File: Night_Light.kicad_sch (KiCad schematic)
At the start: 6 parts, among them Q1 2N3904

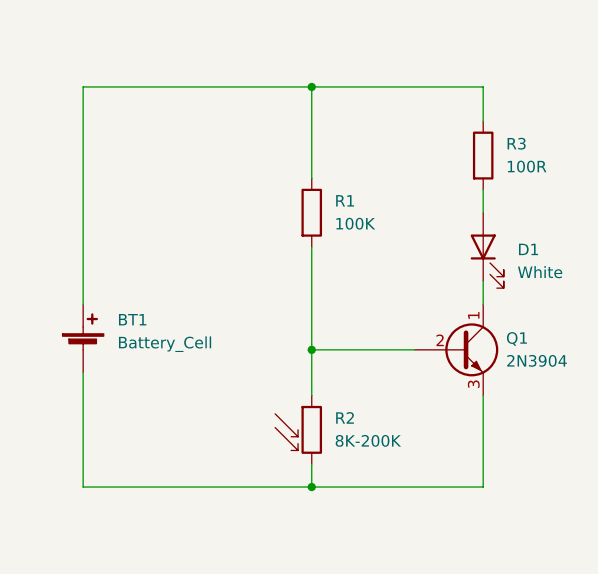
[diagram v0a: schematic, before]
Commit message: Switched battery for connector, add labels, add power flags
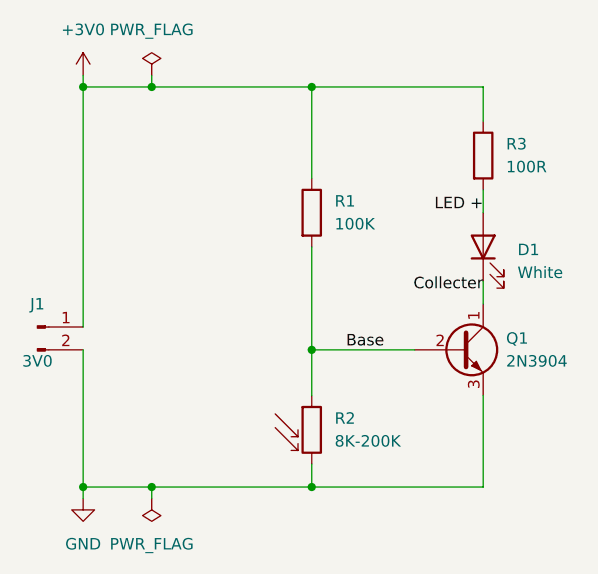
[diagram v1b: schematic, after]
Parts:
- removed BT1: Battery_Cell, symbol Device:Battery_Cell
- added J1: 3V0, symbol Connector:Conn_01x02_Male
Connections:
- net Base: now reaches Q1.2 (B), R1.2, R2.1
- net GND: now reaches Q1.3 (E), R2.2
- net GND: now also J1.2 (Pin_2)
- net Collecter: now reaches D1.1 (K), Q1.1 (C)
- net LED +: now reaches D1.2 (A), R3.2
- net +3V0: now reaches R1.1, R3.1
- net +3V0: now also J1.1 (Pin_1)
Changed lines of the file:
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@@
     (company "Zach Dribin")
   )
+  (junction (at 68.58 88.9) (diameter 0) (color 0 0 0 0)
+  )
   (junction (at 86.36 88.9) (diameter 0) (color 0 0 0 0)
   )
   (junction (at 86.36 133.35) (diameter 0) (color 0 0 0 0)
   )
+  (junction (at 60.96 133.35) (diameter 0) (color 0 0 0 0)
+  )
   (junction (at 86.36 118.11) (diameter 0) (color 0 0 0 0)
   )
+  (junction (at 68.58 133.35) (diameter 0) (color 0 0 0 0)
+  )
+  (junction (at 60.96 88.9) (diameter 0) (color 0 0 0 0)
+  )
   (wire (pts (xy 105.41 110.49) (xy 105.41 113.03))
     (stroke (width 0) (type default) (color 0 0 0 0))
   )
+  (wire (pts (xy 68.58 133.35) (xy 60.96 133.35))
+    (stroke (width 0) (type default) (color 0 0 0 0))
+  )
   (wire (pts (xy 105.41 133.35) (xy 86.36 133.35))
     (stroke (width 0) (type default) (color 0 0 0 0))
@@
     (stroke (width 0) (type default) (color 0 0 0 0))
   )
+  (wire (pts (xy 68.58 133.35) (xy 68.58 134.62))
+    (stroke (width 0) (type default) (color 0 0 0 0))
+  )
   (wire (pts (xy 86.36 106.68) (xy 86.36 118.11))
     (stroke (width 0) (type default) (color 0 0 0 0))
   )
-  (wire (pts (xy 60.96 88.9) (xy 60.96 113.03))
+  (wire (pts (xy 60.96 88.9) (xy 60.96 115.57))
     (stroke (width 0) (type default) (color 0 0 0 0))
   )
@@
     (stroke (width 0) (type default) (color 0 0 0 0))
   )
-  (wire (pts (xy 86.36 133.35) (xy 60.96 133.35))
+  (wire (pts (xy 86.36 133.35) (xy 68.58 133.35))
     (stroke (width 0) (type default) (color 0 0 0 0))
   )
@@
     (stroke (width 0) (type default) (color 0 0 0 0))
   )
+  (wire (pts (xy 68.58 88.9) (xy 86.36 88.9))
+    (stroke (width 0) (type default) (color 0 0 0 0))
+  )
   (wire (pts (xy 86.36 88.9) (xy 86.36 99.06))
     (stroke (width 0) (type default) (color 0 0 0 0))
   )
-  (wire (pts (xy 60.96 88.9) (xy 86.36 88.9))
+  (wire (pts (xy 60.96 88.9) (xy 68.58 88.9))
     (stroke (width 0) (type default) (color 0 0 0 0))
   )
@@
     (stroke (width 0) (type default) (color 0 0 0 0))
   )
+  (wire (pts (xy 60.96 133.35) (xy 60.96 134.62))
+    (stroke (width 0) (type default) (color 0 0 0 0))
+  )
+  (wire (pts (xy 60.96 87.63) (xy 60.96 88.9))
+    (stroke (width 0) (type default) (color 0 0 0 0))
+  )
+  (wire (pts (xy 68.58 87.63) (xy 68.58 88.9))
+    (stroke (width 0) (type default) (color 0 0 0 0))
+  )
   (wire (pts (xy 105.41 123.19) (xy 105.41 133.35))
     (stroke (width 0) (type default) (color 0 0 0 0))
@@
     (stroke (width 0) (type default) (color 0 0 0 0))
   )
-  (wire (pts (xy 60.96 133.35) (xy 60.96 120.65))
-    (stroke (width 0) (type default) (color 0 0 0 0))
+  (wire (pts (xy 60.96 118.11) (xy 60.96 133.35))
+    (stroke (width 0) (type default) (color 0 0 0 0))
+  )
+  (label "LED +" (at 105.41 102.87 180)
+    (effects (font (size 1.27 1.27)) (justify right bottom))
+  )
+  (label "Base" (at 90.17 118.11 0)
+    (effects (font (size 1.27 1.27)) (justify left bottom))
+  )
+  (label "Collecter" (at 105.41 111.76 180)
+    (effects (font (size 1.27 1.27)) (justify right bottom))
+  )
+  (symbol (lib_id "power:PWR_FLAG") (at 68.58 134.62 180) (unit 1)
+    (in_bom yes) (on_board yes) (fields_autoplaced)
+    (property "Reference" "#FLG0101" (id 0) (at 68.58 136.525 0)
+      (effects (font (size 1.27 1.27)) hide)
+    )
+    (property "Value" "PWR_FLAG" (id 1) (at 68.58 139.7 0))
+    (property "Footprint" "" (id 2) (at 68.58 134.62 0)
+      (effects (font (size 1.27 1.27)) hide)
+    )
+    (property "Datasheet" "~" (id 3) (at 68.58 134.62 0)
+      (effects (font (size 1.27 1.27)) hide)
+    )
+    (pin "1")
   )
   (symbol (lib_id "Device:R_Photo") (at 86.36 127 0) (unit 1)
@@
     (pin "3")
   )
+  (symbol (lib_id "power:PWR_FLAG") (at 68.58 87.63 0) (unit 1)
+    (in_bom yes) (on_board yes) (fields_autoplaced)
+    (property "Reference" "#FLG0102" (id 0) (at 68.58 85.725 0)
+      (effects (font (size 1.27 1.27)) hide)
+    )
+    (property "Value" "PWR_FLAG" (id 1) (at 68.58 82.55 0))
+    (property "Footprint" "" (id 2) (at 68.58 87.63 0)
+      (effects (font (size 1.27 1.27)) hide)
+    )
+    (property "Datasheet" "~" (id 3) (at 68.58 87.63 0)
+      (effects (font (size 1.27 1.27)) hide)
+    )
+    (pin "1")
+  )
+  (symbol (lib_id "Connector:Conn_01x02_Male") (at 55.88 115.57 0) (unit 1)
+    (in_bom yes) (on_board yes)
+    (property "Reference" "J1" (id 0) (at 55.88 113.03 0))
+    (property "Value" "3V0" (id 1) (at 55.88 119.38 0))
+    (property "Footprint" "" (id 2) (at 55.88 115.57 0)
+      (effects (font (size 1.27 1.27)) hide)
+    )
+    (property "Datasheet" "~" (id 3) (at 55.88 115.57 0)
+      (effects (font (size 1.27 1.27)) hide)
+    )
+    (pin "1")
+    (pin "2")
+  )
   (symbol (lib_id "Device:R") (at 86.36 102.87 0) (unit 1)
     (in_bom yes) (on_board yes) (fields_autoplaced)
@@
     (pin "2")
   )
-  (symbol (lib_id "Device:Battery_Cell") (at 60.96 118.11 0) (unit 1)
-    (in_bom yes) (on_board yes) (fields_autoplaced)
-    (property "Reference" "BT1" (id 0) (at 64.77 114.8079 0)
-      (effects (font (size 1.27 1.27)) (justify left))
-    )
-    (property "Value" "Battery_Cell" (id 1) (at 64.77 117.3479 0)
-      (effects (font (size 1.27 1.27)) (justify left))
-    )
-    (property "Footprint" "" (id 2) (at 60.96 116.586 90)
-      (effects (font (size 1.27 1.27)) hide)
-    )
-    (property "Datasheet" "~" (id 3) (at 60.96 116.586 90)
-      (effects (font (size 1.27 1.27)) hide)
-    )
-    (pin "1")
-    (pin "2")
+  (symbol (lib_id "power:GND") (at 60.96 134.62 0) (unit 1)
+    (in_bom yes) (on_board yes) (fields_autoplaced)
+    (property "Reference" "#PWR0102" (id 0) (at 60.96 140.97 0)
+      (effects (font (size 1.27 1.27)) hide)
+    )
+    (property "Value" "GND" (id 1) (at 60.96 139.7 0))
+    (property "Footprint" "" (id 2) (at 60.96 134.62 0)
+      (effects (font (size 1.27 1.27)) hide)
+    )
+    (property "Datasheet" "" (id 3) (at 60.96 134.62 0)
+      (effects (font (size 1.27 1.27)) hide)
+    )
+    (pin "1")
+  )
+  (symbol (lib_id "power:+3V0") (at 60.96 87.63 0) (unit 1)
+    (in_bom yes) (on_board yes) (fields_autoplaced)
+    (property "Reference" "#PWR0101" (id 0) (at 60.96 91.44 0)
+      (effects (font (size 1.27 1.27)) hide)
+    )
+    (property "Value" "+3V0" (id 1) (at 60.96 82.55 0))
+    (property "Footprint" "" (id 2) (at 60.96 87.63 0)
+      (effects (font (size 1.27 1.27)) hide)
+    )
+    (property "Datasheet" "" (id 3) (at 60.96 87.63 0)
+      (effects (font (size 1.27 1.27)) hide)
+    )
+    (pin "1")
   )
   (symbol (lib_id "Device:R") (at 105.41 96.52 0) (unit 1)
@@
   )
   (symbol_instances
-    (path "/d35577b0-b0d5-47b7-b305-87b034206361"
-      (reference "BT1") (unit 1) (value "Battery_Cell") (footprint "")
+    (path "/1293d403-3ba4-44cf-b980-8caac3a85bbf"
+      (reference "#FLG0101") (unit 1) (value "PWR_FLAG") (footprint "")
+    )
+    (path "/43f7f27b-9ded-4933-9ad6-9de52f9cb278"
+      (reference "#FLG0102") (unit 1) (value "PWR_FLAG") (footprint "")
+    )
+    (path "/e5c6d5bb-466c-4b56-955c-eded7ca6729a"
+      (reference "#PWR0101") (unit 1) (value "+3V0") (footprint "")
+    )
+    (path "/c92f09ec-5fca-480c-a37c-5597c33419ef"
+      (reference "#PWR0102") (unit 1) (value "GND") (footprint "")
     )
     (path "/201e5f28-9ec4-4f2a-9a4a-06c931c99678"
       (reference "D1") (unit 1) (value "White") (footprint "")
     )
+    (path "/47e2e0a1-3a67-409e-ac27-e47ce2e08aac"
+      (reference "J1") (unit 1) (value "3V0") (footprint "")
+    )
     (path "/21529b31-fbed-4aa1-8161-987b99b8bb72"

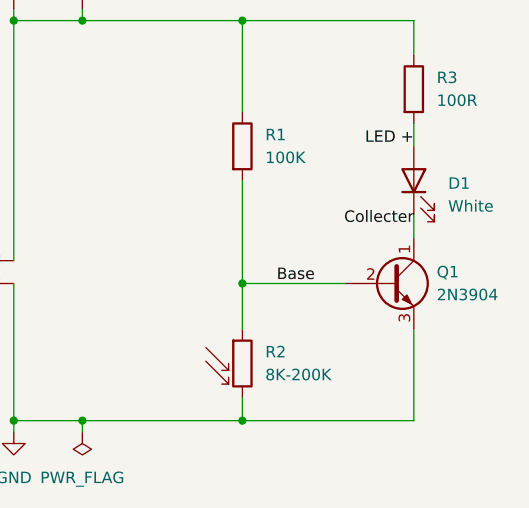
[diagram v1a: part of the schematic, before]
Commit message: Assign all footprints
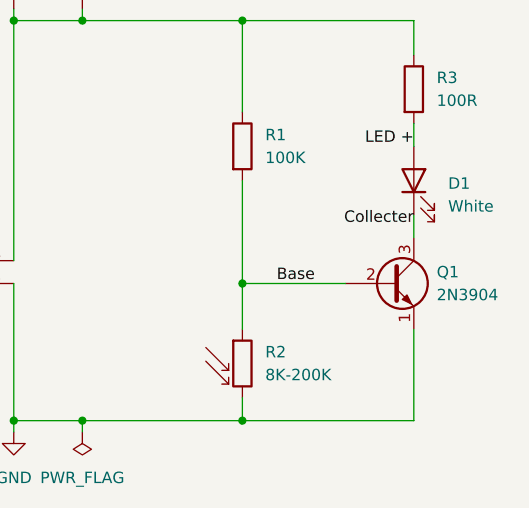
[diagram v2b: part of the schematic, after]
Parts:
- D1: footprint (none) -> LED_THT:LED_D5.0mm_Clear
- J1: footprint (none) -> Connector_Wire:SolderWire-2sqmm_1x02_P7.8mm_D2mm_OD3.9mm
- Q1: footprint (none) -> Package_TO_SOT_THT:TO-92_HandSolder; symbol Device:Q_NPN_CBE -> Device:Q_NPN_EBC
- R1, R3: footprint (none) -> Resistor_THT:R_Axial_DIN0207_L6.3mm_D2.5mm_P10.16mm_Horizontal
- R2: footprint (none) -> OptoDevice:R_LDR_4.9x4.2mm_P2.54mm_Vertical
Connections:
- net Collecter: now also Q1.3 (C); no longer Q1.1 (C)
- net GND: now also Q1.1 (E); no longer Q1.3 (E)
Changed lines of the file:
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@@
       (effects (font (size 1.27 1.27)) (justify left))
     )
-    (property "Footprint" "" (id 2) (at 87.63 133.35 90)
+    (property "Footprint" "OptoDevice:R_LDR_4.9x4.2mm_P2.54mm_Vertical" (id 2) (at 87.63 133.35 90)
       (effects (font (size 1.27 1.27)) (justify left) hide)
     )
@@
       (effects (font (size 1.27 1.27)) (justify right))
     )
-    (property "Footprint" "" (id 2) (at 105.41 106.68 0)
+    (property "Footprint" "LED_THT:LED_D5.0mm_Clear" (id 2) (at 105.41 106.68 0)
       (effects (font (size 1.27 1.27)) hide)
     )
@@
     (pin "2")
   )
-  (symbol (lib_id "Device:Q_NPN_CBE") (at 102.87 118.11 0) (unit 1)
+  (symbol (lib_id "Device:Q_NPN_EBC") (at 102.87 118.11 0) (unit 1)
     (in_bom yes) (on_board yes) (fields_autoplaced)
     (property "Reference" "Q1" (id 0) (at 107.95 116.8399 0)
@@
       (effects (font (size 1.27 1.27)) (justify left))
     )
-    (property "Footprint" "" (id 2) (at 107.95 115.57 0)
+    (property "Footprint" "Package_TO_SOT_THT:TO-92_HandSolder" (id 2) (at 107.95 115.57 0)
       (effects (font (size 1.27 1.27)) hide)
     )
@@
     (property "Reference" "J1" (id 0) (at 55.88 113.03 0))
     (property "Value" "3V0" (id 1) (at 55.88 119.38 0))
-    (property "Footprint" "" (id 2) (at 55.88 115.57 0)
+    (property "Footprint" "Connector_Wire:SolderWire-2sqmm_1x02_P7.8mm_D2mm_OD3.9mm" (id 2) (at 55.88 115.57 0)
       (effects (font (size 1.27 1.27)) hide)
     )
@@
       (effects (font (size 1.27 1.27)) (justify left))
     )
-    (property "Footprint" "" (id 2) (at 84.582 102.87 90)
+    (property "Footprint" "Resistor_THT:R_Axial_DIN0207_L6.3mm_D2.5mm_P10.16mm_Horizontal" (id 2) (at 84.582 102.87 90)
       (effects (font (size 1.27 1.27)) hide)
     )
@@
       (effects (font (size 1.27 1.27)) (justify left))
     )
-    (property "Footprint" "" (id 2) (at 103.632 96.52 90)
+    (property "Footprint" "Resistor_THT:R_Axial_DIN0207_L6.3mm_D2.5mm_P10.16mm_Horizontal" (id 2) (at 103.632 96.52 90)
       (effects (font (size 1.27 1.27)) hide)
     )
@@
     )
     (path "/201e5f28-9ec4-4f2a-9a4a-06c931c99678"
-      (reference "D1") (unit 1) (value "White") (footprint "")
+      (reference "D1") (unit 1) (value "White") (footprint "LED_THT:LED_D5.0mm_Clear")
     )
     (path "/47e2e0a1-3a67-409e-ac27-e47ce2e08aac"
-      (reference "J1") (unit 1) (value "3V0") (footprint "")
+      (reference "J1") (unit 1) (value "3V0") (footprint "Connector_Wire:SolderWire-2sqmm_1x02_P7.8mm_D2mm_OD3.9mm")
     )
     (path "/21529b31-fbed-4aa1-8161-987b99b8bb72"
-      (reference "Q1") (unit 1) (value "2N3904") (footprint "")
+      (reference "Q1") (unit 1) (value "2N3904") (footprint "Package_TO_SOT_THT:TO-92_HandSolder")
     )
     (path "/88e923cf-fa2e-4fa3-9130-af5a72349912"
-      (reference "R1") (unit 1) (value "100K") (footprint "")
+      (reference "R1") (unit 1) (value "100K") (footprint "Resistor_THT:R_Axial_DIN0207_L6.3mm_D2.5mm_P10.16mm_Horizontal")
     )
     (path "/18d72c6c-48f1-4f58-b4bd-603b0d4cbbcb"
-      (reference "R2") (unit 1) (value "8K-200K") (footprint "")
+      (reference "R2") (unit 1) (value "8K-200K") (footprint "OptoDevice:R_LDR_4.9x4.2mm_P2.54mm_Vertical")
     )
     (path "/efe1dff2-774b-43d6-b07c-abd5c4f91b66"
-      (reference "R3") (unit 1) (value "100R") (footprint "")
+      (reference "R3") (unit 1) (value "100R") (footprint "Resistor_THT:R_Axial_DIN0207_L6.3mm_D2.5mm_P10.16mm_Horizontal")
     )
   )

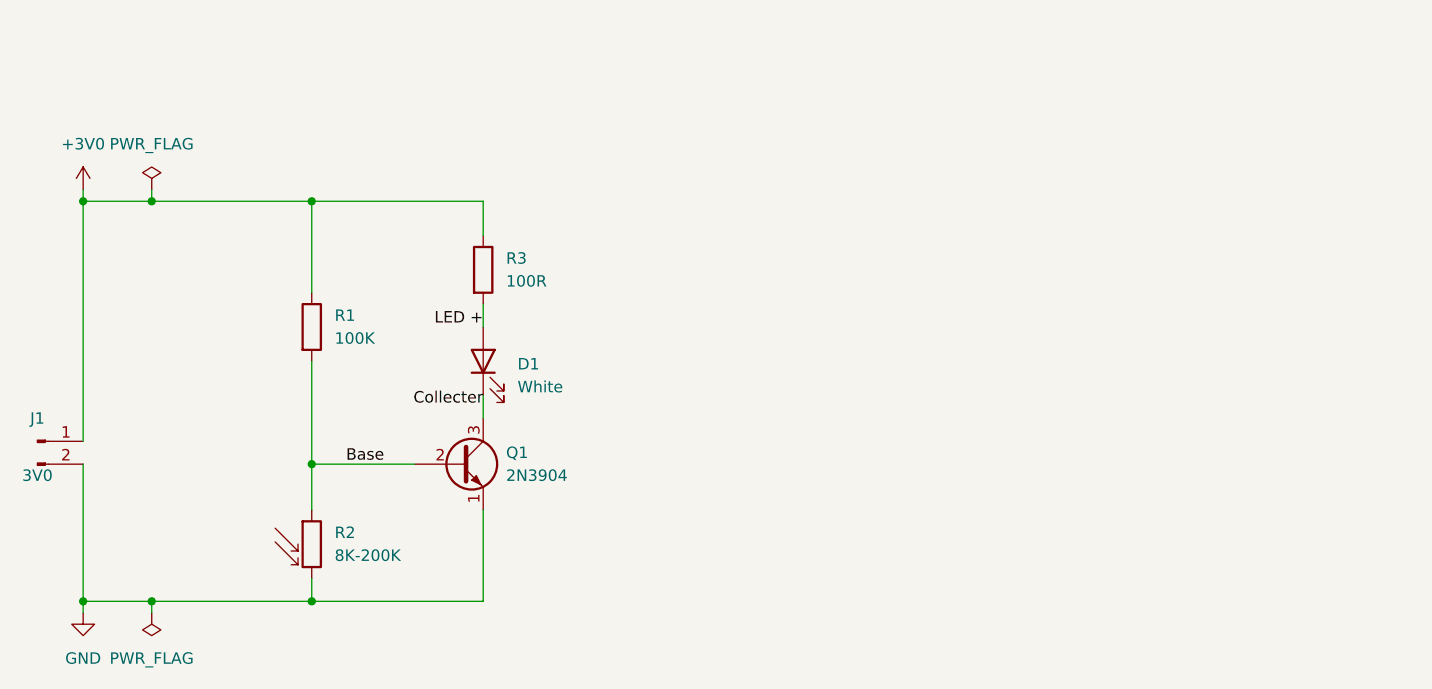
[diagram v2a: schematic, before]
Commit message: Initial board layout. No traces.
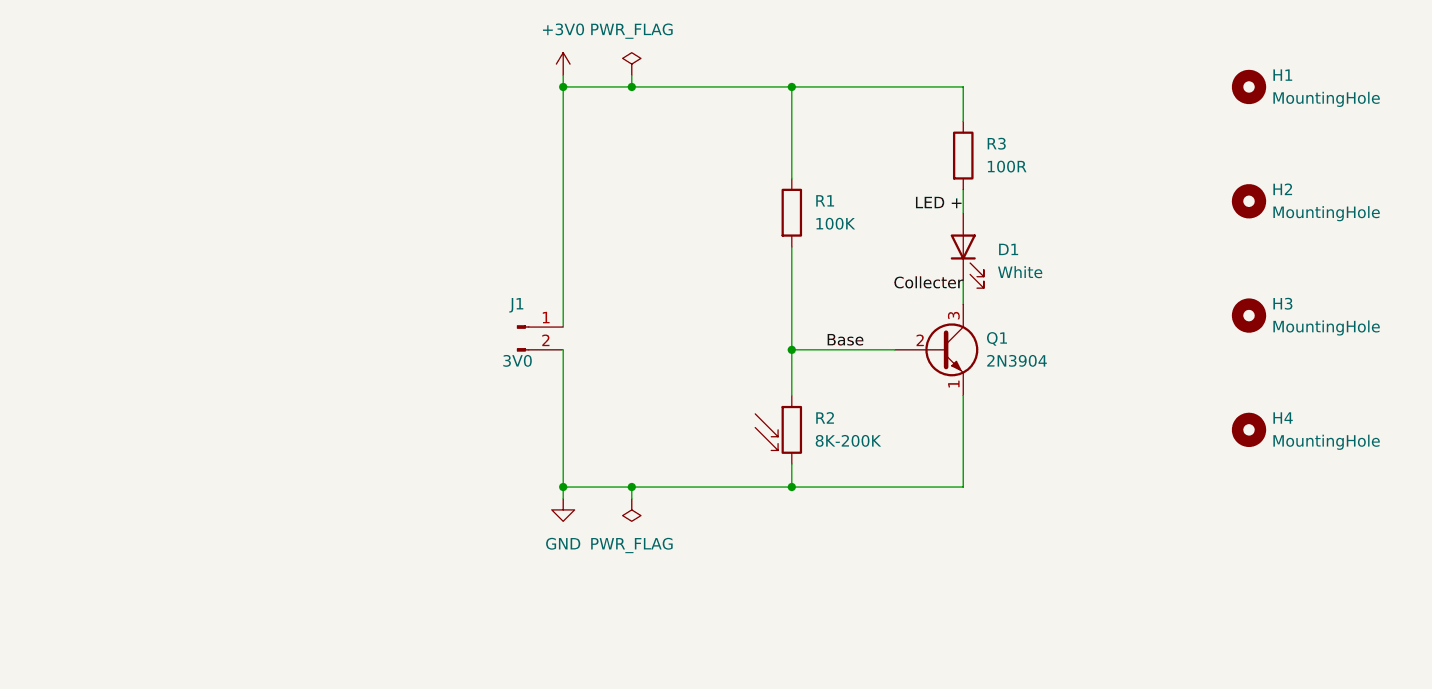
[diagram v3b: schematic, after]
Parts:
- added H1, H2, H3, H4: MountingHole, MountingHole:MountingHole_3.2mm_M3, symbol Mechanical:MountingHole
- J1: footprint Connector_Wire:SolderWire-2sqmm_1x02_P7.8mm_D2mm_OD3.9mm -> Connector_Wire:SolderWire-1.5sqmm_1x02_P6mm_D1.7mm_OD3mm
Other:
- moved on the sheet: D1, J1, Q1, R1, R2, R3
